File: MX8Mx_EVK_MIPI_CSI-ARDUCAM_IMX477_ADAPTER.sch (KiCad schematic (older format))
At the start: 12 parts, among them J1 1888863-4, J2 54548-2271, U1 NLSX5012DMR2G, U2 PCA9306D

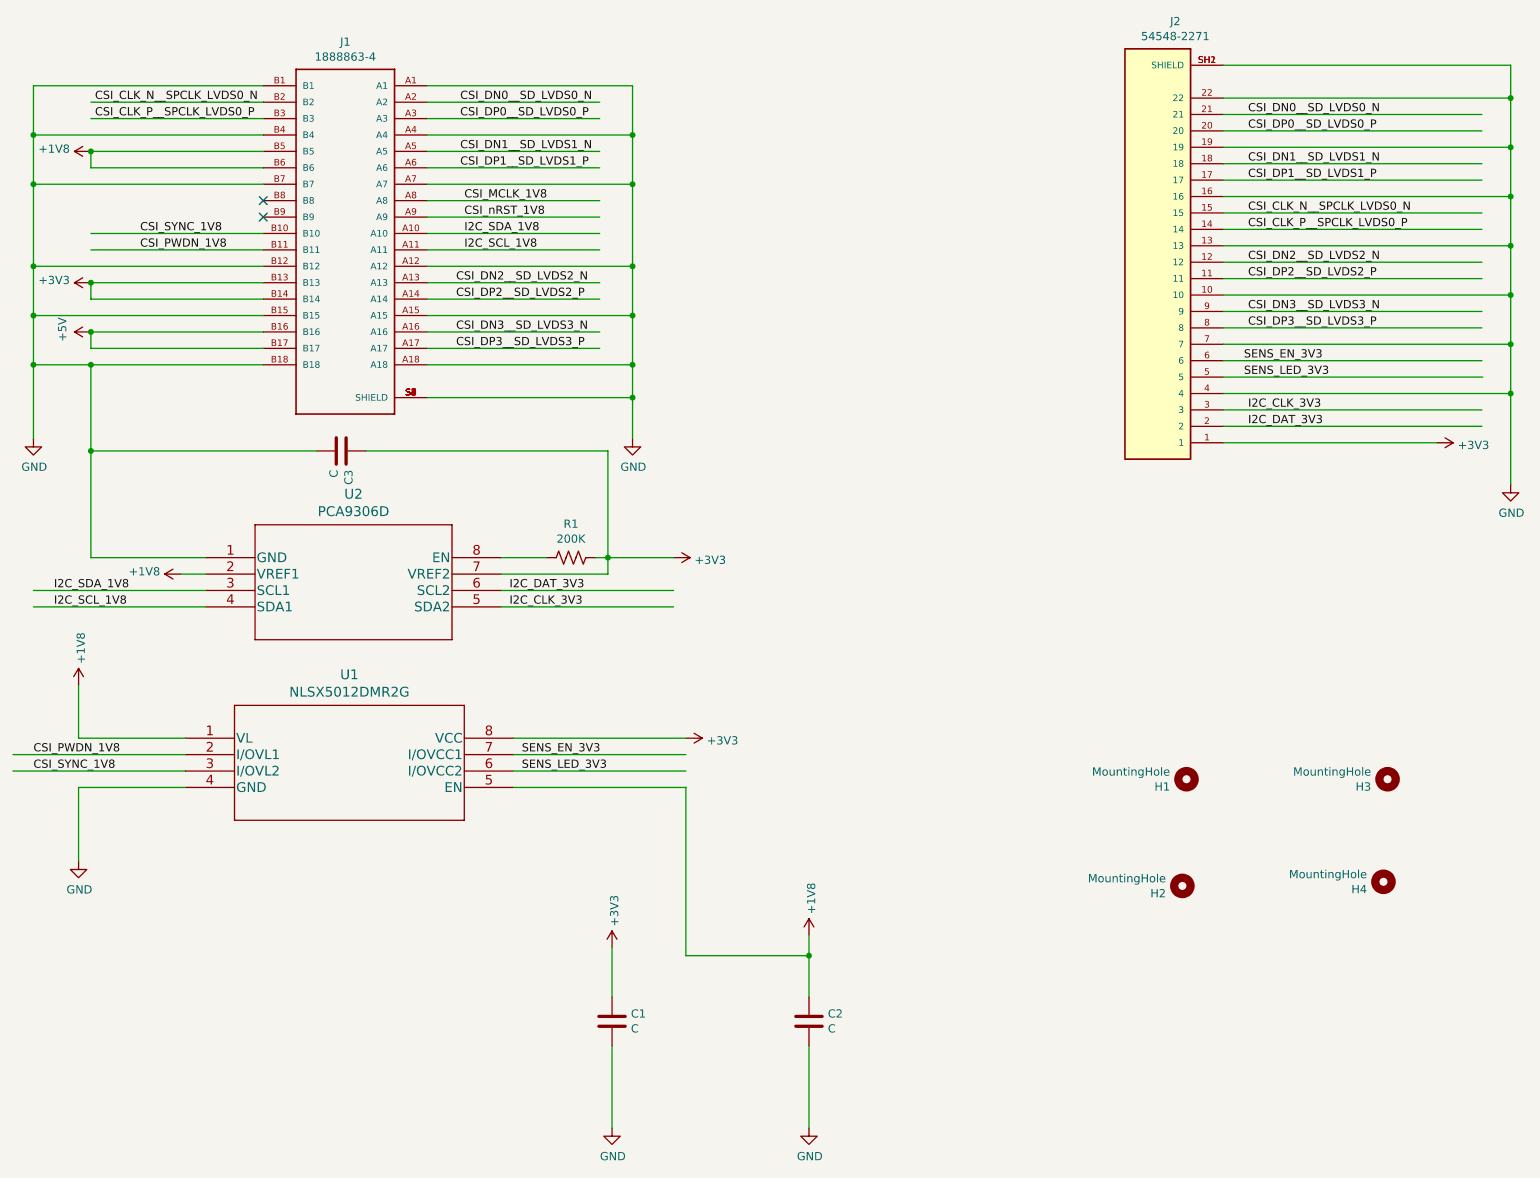
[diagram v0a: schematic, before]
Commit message: Add option to select 1V8/3V3 level for signals of camera side
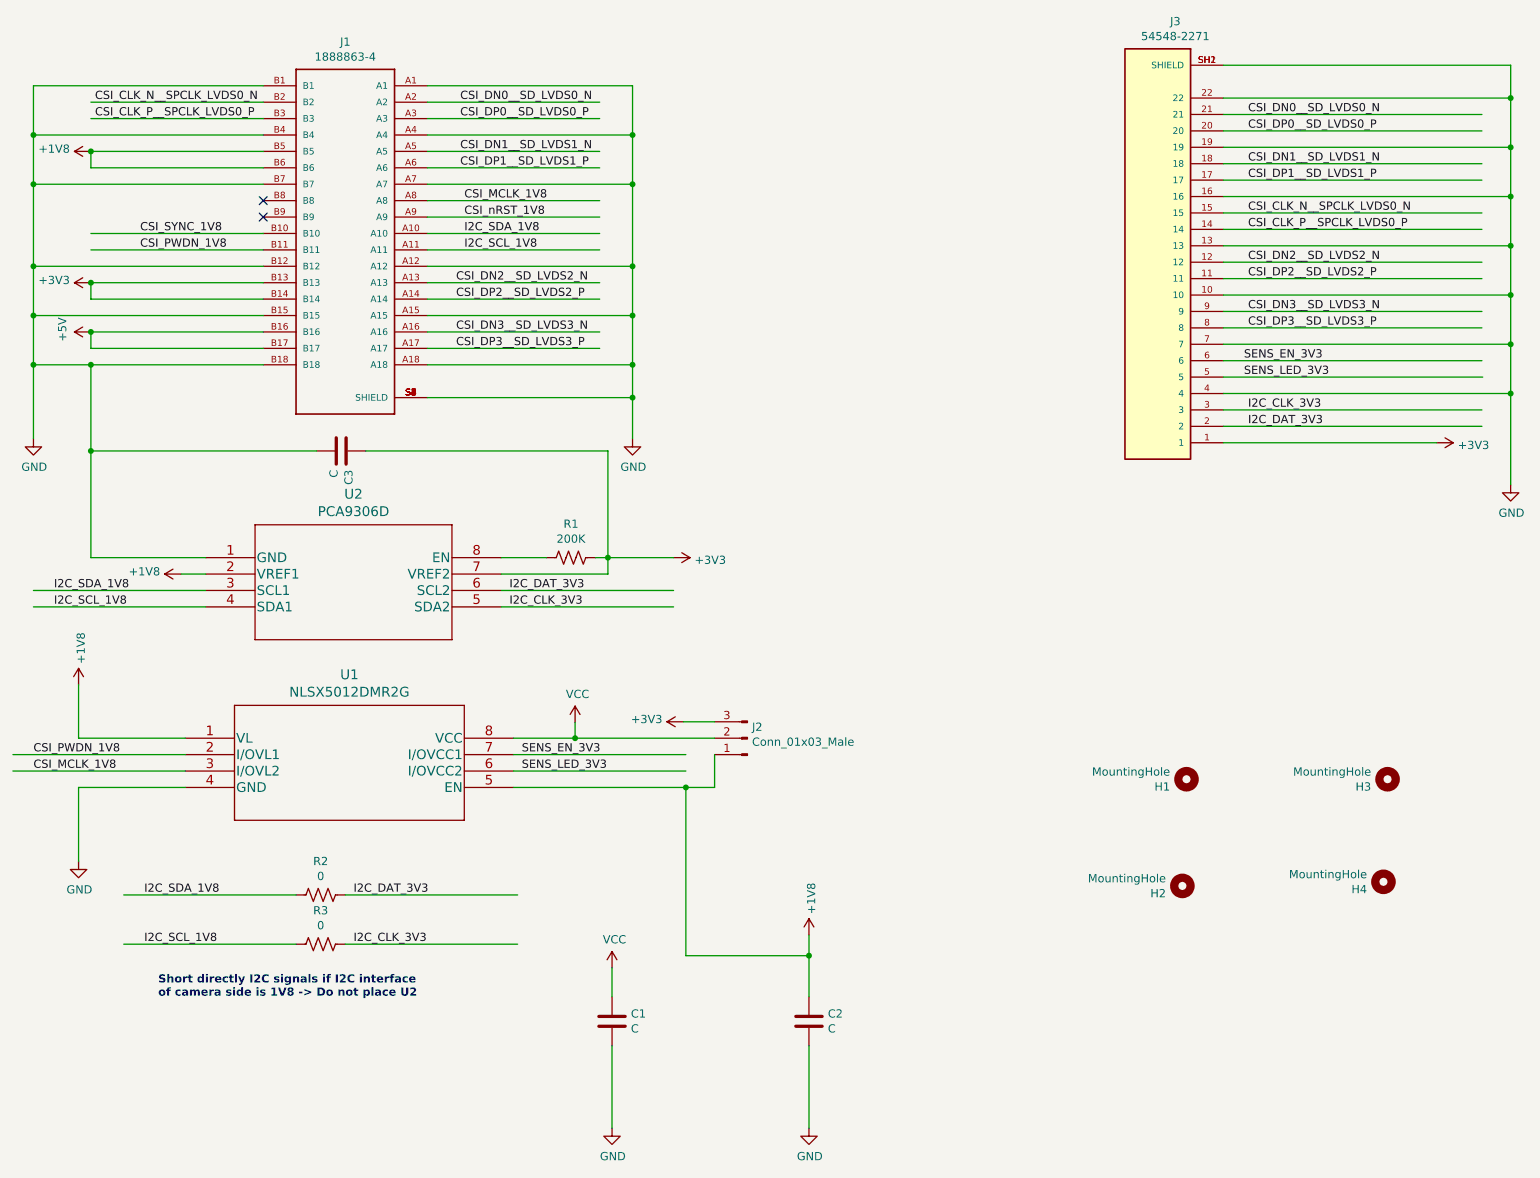
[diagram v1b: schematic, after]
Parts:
- added J2: Conn_01x03_Male, Connector_PinHeader_2.54mm:PinHeader_1x03_P2.54mm_Vertical, symbol Connector:Conn_01x03_Male
- added R2, R3: 0, Resistor_SMD:R_0603_1608Metric_Pad0.98x0.95mm_HandSolder, symbol Device:R_US
- renumbered J2 to J3
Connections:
- net labels added: VCC
- wire segments 116 -> 125
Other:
- note added: "Short directly I2C signals if I2C interface \nof camera side is 1V8 -> Do not place U2"
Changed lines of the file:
@@
 I2C_SCL_1V8
-$Comp
-L power:+3V3 #PWR0112
-U 1 1 615AC6B3
-P 4825 5050
-F 0 "#PWR0112" H 4825 4900 50  0001 C CNN
-F 1 "+3V3" V 4840 5178 50  0000 L CNN
-F 2 "" H 4825 5050 50  0001 C CNN
-F 3 "" H 4825 5050 50  0001 C CNN
-	1    4825 5050
-	0    1    1    0
-$EndComp
 $Comp
 L power:+1V8 #PWR0113
@@
 SENS_LED_3V3
 $Comp
-L Device:C C1
-U 1 1 619130F9
-P 4375 6775
-F 0 "C1" H 4490 6821 50  0000 L CNN
-F 1 "C" H 4490 6730 50  0000 L CNN
-F 2 "Capacitor_SMD:C_0603_1608Metric_Pad1.08x0.95mm_HandSolder" H 4413 6625 50  0001 C CNN
-F 3 "~" H 4375 6775 50  0001 C CNN
-	1    4375 6775
-	1    0    0    -1
-$EndComp
-$Comp
-L power:GND #PWR0106
-U 1 1 619522BB
-P 4375 7425
-F 0 "#PWR0106" H 4375 7175 50  0001 C CNN
-F 1 "GND" H 4380 7252 50  0000 C CNN
-F 2 "" H 4375 7425 50  0001 C CNN
-F 3 "" H 4375 7425 50  0001 C CNN
-	1    4375 7425
-	1    0    0    -1
-$EndComp
-Wire Wire Line
-	4375 6925 4375 7425
-$Comp
-L power:+3V3 #PWR0107
-U 1 1 61966ED2
-P 4375 6325
-F 0 "#PWR0107" H 4375 6175 50  0001 C CNN
-F 1 "+3V3" V 4390 6453 50  0000 L CNN
-F 2 "" H 4375 6325 50  0001 C CNN
-F 3 "" H 4375 6325 50  0001 C CNN
-	1    4375 6325
-	1    0    0    -1
-$EndComp
-Wire Wire Line
-	4375 6325 4375 6625
-$Comp
-L Device:C C2
-U 1 1 619778C4
-P 5575 6775
-F 0 "C2" H 5690 6821 50  0000 L CNN
-F 1 "C" H 5690 6730 50  0000 L CNN
-F 2 "Capacitor_SMD:C_0603_1608Metric_Pad1.08x0.95mm_HandSolder" H 5613 6625 50  0001 C CNN
-F 3 "~" H 5575 6775 50  0001 C CNN
-	1    5575 6775
-	1    0    0    -1
-$EndComp
-$Comp
 L power:GND #PWR0117
 U 1 1 619778CA
@@
 Wire Wire Line
 	4300 1275 3250 1275
-Wire Wire Line
-	3775 5050 4825 5050
 NoConn ~ 2250 1775
 NoConn ~ 2250 1875
@@
 $EndComp
 Text Label 850  5250 0    50   ~ 0
-CSI_SYNC_1V8
+CSI_MCLK_1V8
 Text Label 850  5150 0    50   ~ 0
 CSI_PWDN_1V8
@@
 	8100 1950 9675 1950
 $Comp
-L 54548-2271:54548-2271 J2
+L 54548-2271:54548-2271 J3
 U 1 1 627DEC01
 P 7700 2150
-F 0 "J2" H 7593 683 50  0000 C CNN
+F 0 "J3" H 7593 683 50  0000 C CNN
 F 1 "54548-2271" H 7593 774 50  0000 C CNN
 F 2 "footprints:MOLEX_54548-2271" H 7700 2150 50  0001 L BNN
@@
 	9850 950  9850 1150
 Connection ~ 9850 1150
+$Comp
+L Device:R_US R2
+U 1 1 627DBFD9
+P 2600 6005
+F 0 "R2" V 2395 6005 50  0000 C CNN
+F 1 "0" V 2486 6005 50  0000 C CNN
+F 2 "Resistor_SMD:R_0603_1608Metric_Pad0.98x0.95mm_HandSolder" V 2640 5995 50  0001 C CNN
+F 3 "~" H 2600 6005 50  0001 C CNN
+	1    2600 6005
+	0    1    1    0
+$EndComp
+$Comp
+L Device:R_US R3
+U 1 1 627E4AC0
+P 2600 6305
+F 0 "R3" V 2395 6305 50  0000 C CNN
+F 1 "0" V 2486 6305 50  0000 C CNN
+F 2 "Resistor_SMD:R_0603_1608Metric_Pad0.98x0.95mm_HandSolder" V 2640 6295 50  0001 C CNN
+F 3 "~" H 2600 6305 50  0001 C CNN
+	1    2600 6305
+	0    1    1    0
+$EndComp
+Wire Wire Line
+	3800 6305 2750 6305
+Wire Wire Line
+	3800 6005 2750 6005
+Text Label 2800 6005 0    50   ~ 0
+I2C_DAT_3V3
+Text Label 2800 6305 0    50   ~ 0
+I2C_CLK_3V3
+Wire Wire Line
+	2450 6305 1400 6305
+Wire Wire Line
+	2450 6005 1400 6005
+Text Label 1525 6305 0    50   ~ 0
+I2C_SCL_1V8
+Text Label 1525 6005 0    50   ~ 0
+I2C_SDA_1V8
+$Comp
+L Connector:Conn_01x03_Male J2
+U 1 1 62829930
+P 5200 5050
+F 0 "J2" H 5172 4982 50  0000 R CNN
+F 1 "Conn_01x03_Male" H 5172 5073 50  0000 R CNN
+F 2 "Connector_PinHeader_2.54mm:PinHeader_1x03_P2.54mm_Vertical" H 5200 5050 50  0001 C CNN
+F 3 "~" H 5200 5050 50  0001 C CNN
+	1    5200 5050
+	-1   0    0    1
+$EndComp
+Wire Wire Line
+	5000 5050 4150 5050
+$Comp
+L power:+3V3 #PWR0112
+U 1 1 6287F34A
+P 4810 4950
+F 0 "#PWR0112" H 4810 4800 50  0001 C CNN
+F 1 "+3V3" V 4825 5078 50  0000 L CNN
+F 2 "" H 4810 4950 50  0001 C CNN
+F 3 "" H 4810 4950 50  0001 C CNN
+	1    4810 4950
+	0    -1   -1   0
+$EndComp
+Wire Wire Line
+	4810 4950 5000 4950
+Wire Wire Line
+	5000 5150 5000 5350
+Wire Wire Line
+	5000 5350 4825 5350
+Connection ~ 4825 5350
+Text Notes 1610 6635 0    50   ~ 10
+Short directly I2C signals if I2C interface \nof camera side is 1V8 -> Do not place U2
+$Comp
+L Device:C C2
+U 1 1 619778C4
+P 5575 6775
+F 0 "C2" H 5690 6821 50  0000 L CNN
+F 1 "C" H 5690 6730 50  0000 L CNN
+F 2 "Capacitor_SMD:C_0603_1608Metric_Pad1.08x0.95mm_HandSolder" H 5613 6625 50  0001 C CNN
+F 3 "~" H 5575 6775 50  0001 C CNN
+	1    5575 6775
+	1    0    0    -1
+$EndComp
+$Comp
+L power:GND #PWR0106
+U 1 1 619522BB
+P 4375 7425
+F 0 "#PWR0106" H 4375 7175 50  0001 C CNN
+F 1 "GND" H 4380 7252 50  0000 C CNN
+F 2 "" H 4375 7425 50  0001 C CNN
+F 3 "" H 4375 7425 50  0001 C CNN
+	1    4375 7425
+	1    0    0    -1
+$EndComp
+Wire Wire Line
+	4375 6925 4375 7425
+$Comp
+L Device:C C1
+U 1 1 619130F9
+P 4375 6775
+F 0 "C1" H 4490 6821 50  0000 L CNN
+F 1 "C" H 4490 6730 50  0000 L CNN
+F 2 "Capacitor_SMD:C_0603_1608Metric_Pad1.08x0.95mm_HandSolder" H 4413 6625 50  0001 C CNN
+F 3 "~" H 4375 6775 50  0001 C CNN
+	1    4375 6775
+	1    0    0    -1
+$EndComp
+$Comp
+L power:VCC #PWR0107
+U 1 1 628BC739
+P 4375 6450
+F 0 "#PWR0107" H 4375 6300 50  0001 C CNN
+F 1 "VCC" H 4390 6623 50  0000 C CNN
+F 2 "" H 4375 6450 50  0001 C CNN
+F 3 "" H 4375 6450 50  0001 C CNN
+	1    4375 6450
+	1    0    0    -1
+$EndComp
+Wire Wire Line
+	4375 6625 4375 6450
+$Comp
+L power:VCC #PWR0115
+U 1 1 628D329F
+P 4150 4955
+F 0 "#PWR0115" H 4150 4805 50  0001 C CNN
+F 1 "VCC" H 4165 5128 50  0000 C CNN
+F 2 "" H 4150 4955 50  0001 C CNN
+F 3 "" H 4150 4955 50  0001 C CNN
+	1    4150 4955
+	1    0    0    -1
+$EndComp
+Wire Wire Line
+	4150 4955 4150 5050
+Connection ~ 4150 5050
+Wire Wire Line
+	4150 5050 3775 5050
 $EndSCHEMATC
